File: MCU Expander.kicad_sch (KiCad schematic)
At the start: 0 parts

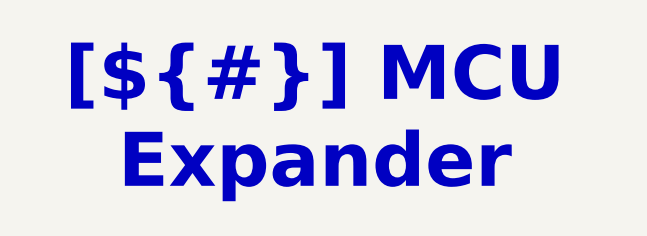
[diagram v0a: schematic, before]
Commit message: [Schematic][Add] Add of a new page : MCU Expander
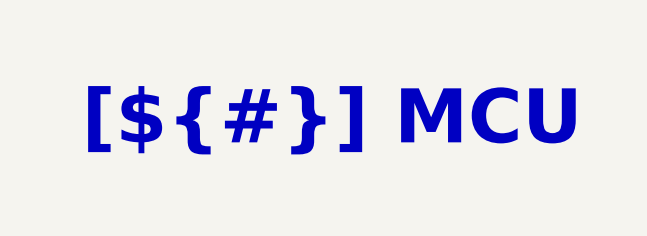
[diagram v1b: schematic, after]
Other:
- title: MCU Expander -> MCU
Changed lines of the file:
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@@
 	(paper "A4")
 	(title_block
-		(title "MCU Expander")
+		(title "MCU")
 		(date "2025-01-12")
 		(rev "${REVISION}")
@@
 	(text_box "[${#}] ${TITLE}"
 		(exclude_from_sim no)
-		(at 102.87 15.24 0)
-		(size 93.98 12.7)
+		(at 115.57 15.24 0)
+		(size 72.39 12.7)
 		(margins 4.4999 4.4999 4.4999 4.4999)
 		(stroke

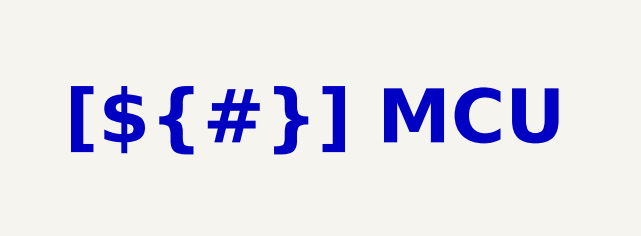
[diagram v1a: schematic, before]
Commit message: [Schematic][Add] MCU
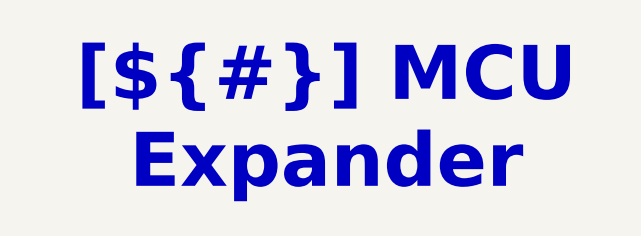
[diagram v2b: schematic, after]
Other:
- title: MCU -> MCU Expander
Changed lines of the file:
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@@
 	(paper "A4")
 	(title_block
-		(title "MCU")
+		(title "MCU Expander")
 		(date "2025-01-12")
 		(rev "${REVISION}")
@@
 	(text_box "[${#}] ${TITLE}"
 		(exclude_from_sim no)
-		(at 115.57 15.24 0)
-		(size 72.39 12.7)
+		(at 109.22 15.24 0)
+		(size 87.63 12.7)
 		(margins 4.4999 4.4999 4.4999 4.4999)
 		(stroke

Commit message: [Schematic][Add] MCU Expander Schematic
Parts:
- added C13, C15, C18: 100nF, Capacitor_SMD:C_0603_1608Metric_Pad1.08x0.95mm_HandSolder, symbol Device:C_Small
- added J2: *, Connector_Molex:Molex_Micro-Fit_3.0_43045-0612_2x03_P3.00mm_Vertical, symbol Connector_Generic:Conn_02x03_Odd_Even
- added R13: 10k, Resistor_SMD:R_0603_1608Metric_Pad0.98x0.95mm_HandSolder, symbol Device:R_Small
- added U2: TCAL9539, Package_SO:TSSOP-24_4.4x7.8mm_P0.65mm, symbol P_Interface:TCA9535PWR
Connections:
- new net +3.3V: C13.1, C18.1, J2.2 (Pin_2), R13.2, U2.24 (VCC)
- new net +5V: C15.1, J2.4 (Pin_4)
- new net CD_RELAY1: U2.10 (P06)
- new net CD_RELAY2: U2.11 (P07)
- new net GND: C13.2, C15.2, C18.2, J2.6 (Pin_6), U2.12 (GND), U2.2 (A1), U2.21 (A0)
- new net GPIO_EXP_P14: U2.17 (P14)
- new net GPIO_EXP_P15: U2.18 (P15)
- new net GPIO_EXP_P16: U2.19 (P16)
- new net GPIO_EXP_P17: U2.20 (P17)
- new net GPIO_Expander_~{INT}: U2.1 (~{INT})
- new net GPIO_Expander_~{RESET}: R13.1, U2.3 (~{RESET})
- new net I2C2_SCL: U2.22 (SCL)
- new net I2C2_SDA: U2.23 (SDA)
- new net IMU_SENSOR_INT1: U2.4 (P00)
- new net IMU_SENSOR_INT2: U2.5 (P01)
- new net Light_SENSOR_INT: U2.6 (P02)
- new net MCU_SPARE1: J2.1 (Pin_1)
- new net MCU_SPARE2: J2.3 (Pin_3)
- new net MicroSD_Detection: U2.7 (P03)
- new net RS485_DE: U2.9 (P05)
- new net RS485_~{RE}: U2.8 (P04)
- new net Switch_DIP_1: U2.13 (P10)
- new net Switch_DIP_2: U2.14 (P11)
- new net Switch_DIP_3: U2.15 (P12)
- new net Switch_DIP_4: U2.16 (P13)
- no-connect marks 0 -> 1

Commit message: [Schematic][Modify] Clear all annotation
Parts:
- renumbered C18 to C?, C13 to C?, C15 to C?, J2 to J?, R13 to R?, U2 to U?
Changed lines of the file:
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@@
 		(on_board yes)
 		(dnp no)
-		(property "Reference" "#PWR049"
+		(property "Reference" "#PWR?"
 			(at 195.58 130.81 0)
 			(effects
@@
 			(project "Data-Acquisition-Board"
 				(path "/f9e05184-c88b-4a88-ae9c-ab2bdb32be7c/c5103ceb-5325-4a84-a025-9638a412984e/6ab43cd8-dabb-49a4-aa94-5d820261f9f9"
-					(reference "#PWR049")
+					(reference "#PWR?")
 					(unit 1)
 				)
@@
 		(on_board yes)
 		(dnp no)
-		(property "Reference" "#PWR024"
+		(property "Reference" "#PWR?"
 			(at 99.06 76.2 0)
 			(effects
@@
 			(project "Data-Acquisition-Board"
 				(path "/f9e05184-c88b-4a88-ae9c-ab2bdb32be7c/c5103ceb-5325-4a84-a025-9638a412984e/6ab43cd8-dabb-49a4-aa94-5d820261f9f9"
-					(reference "#PWR024")
+					(reference "#PWR?")
 					(unit 1)
 				)
@@
 		(on_board yes)
 		(dnp no)
-		(property "Reference" "#PWR032"
+		(property "Reference" "#PWR?"
 			(at 110.49 74.93 0)
 			(effects
@@
 			(project "Data-Acquisition-Board"
 				(path "/f9e05184-c88b-4a88-ae9c-ab2bdb32be7c/c5103ceb-5325-4a84-a025-9638a412984e/6ab43cd8-dabb-49a4-aa94-5d820261f9f9"
-					(reference "#PWR032")
+					(reference "#PWR?")
 					(unit 1)
 				)
@@
 		(on_board yes)
 		(dnp no)
-		(property "Reference" "#PWR047"
+		(property "Reference" "#PWR?"
 			(at 176.53 63.5 0)
 			(effects
@@
 			(project "Data-Acquisition-Board"
 				(path "/f9e05184-c88b-4a88-ae9c-ab2bdb32be7c/c5103ceb-5325-4a84-a025-9638a412984e/6ab43cd8-dabb-49a4-aa94-5d820261f9f9"
-					(reference "#PWR047")
+					(reference "#PWR?")
 					(unit 1)
 				)
@@
 		(on_board yes)
 		(dnp no)
-		(property "Reference" "R13"
+		(property "Reference" "R?"
 			(at 172.466 86.36 0)
 			(effects
@@
 			(project "Data-Acquisition-Board"
 				(path "/f9e05184-c88b-4a88-ae9c-ab2bdb32be7c/c5103ceb-5325-4a84-a025-9638a412984e/6ab43cd8-dabb-49a4-aa94-5d820261f9f9"
-					(reference "R13")
+					(reference "R?")
 					(unit 1)
 				)
@@
 		(on_board yes)
 		(dnp no)
-		(property "Reference" "#PWR048"
+		(property "Reference" "#PWR?"
 			(at 195.58 64.77 0)
 			(effects
@@
 			(project "Data-Acquisition-Board"
 				(path "/f9e05184-c88b-4a88-ae9c-ab2bdb32be7c/c5103ceb-5325-4a84-a025-9638a412984e/6ab43cd8-dabb-49a4-aa94-5d820261f9f9"
-					(reference "#PWR048")
+					(reference "#PWR?")
 					(unit 1)
 				)
@@
 		(on_board yes)
 		(dnp no)
-		(property "Reference" "J2"
+		(property "Reference" "J?"
 			(at 91.44 58.42 0)
 			(effects
@@
 			(project "Data-Acquisition-Board"
 				(path "/f9e05184-c88b-4a88-ae9c-ab2bdb32be7c/c5103ceb-5325-4a84-a025-9638a412984e/6ab43cd8-dabb-49a4-aa94-5d820261f9f9"
-					(reference "J2")
+					(reference "J?")
 					(unit 1)
 				)
@@
 		(on_board yes)
 		(dnp no)
-		(property "Reference" "#PWR028"
+		(property "Reference" "#PWR?"
 			(at 104.14 66.04 0)
 			(effects
@@
 			(project "Data-Acquisition-Board"
 				(path "/f9e05184-c88b-4a88-ae9c-ab2bdb32be7c/c5103ceb-5325-4a84-a025-9638a412984e/6ab43cd8-dabb-49a4-aa94-5d820261f9f9"
-					(reference "#PWR028")
+					(reference "#PWR?")
 					(unit 1)
 				)
@@
 		(on_board yes)
 		(dnp no)
-		(property "Reference" "#PWR031"
+		(property "Reference" "#PWR?"
 			(at 110.49 63.5 0)
 			(effects
@@
 			(project "Data-Acquisition-Board"
 				(path "/f9e05184-c88b-4a88-ae9c-ab2bdb32be7c/c5103ceb-5325-4a84-a025-9638a412984e/6ab43cd8-dabb-49a4-aa94-5d820261f9f9"
-					(reference "#PWR031")
+					(reference "#PWR?")
 					(unit 1)
 				)
@@
 		(on_board yes)
 		(dnp no)
-		(property "Reference" "#PWR046"
+		(property "Reference" "#PWR?"
 			(at 175.26 130.81 0)
 			(effects
@@
 			(project "Data-Acquisition-Board"
 				(path "/f9e05184-c88b-4a88-ae9c-ab2bdb32be7c/c5103ceb-5325-4a84-a025-9638a412984e/6ab43cd8-dabb-49a4-aa94-5d820261f9f9"
-					(reference "#PWR046")
+					(reference "#PWR?")
 					(unit 1)
 				)
@@
 		(on_board yes)
 		(dnp no)
-		(property "Reference" "#PWR023"
+		(property "Reference" "#PWR?"
 			(at 99.06 66.04 0)
 			(effects
@@
 			(project "Data-Acquisition-Board"
 				(path "/f9e05184-c88b-4a88-ae9c-ab2bdb32be7c/c5103ceb-5325-4a84-a025-9638a412984e/6ab43cd8-dabb-49a4-aa94-5d820261f9f9"
-					(reference "#PWR023")
+					(reference "#PWR?")
 					(unit 1)
 				)
@@
 		(on_board yes)
 		(dnp no)
-		(property "Reference" "#PWR037"
+		(property "Reference" "#PWR?"
 			(at 123.19 74.93 0)
 			(effects
@@
 			(project "Data-Acquisition-Board"
 				(path "/f9e05184-c88b-4a88-ae9c-ab2bdb32be7c/c5103ceb-5325-4a84-a025-9638a412984e/6ab43cd8-dabb-49a4-aa94-5d820261f9f9"
-					(reference "#PWR037")
+					(reference "#PWR?")
 					(unit 1)
 				)
@@
 		(on_board yes)
 		(dnp no)
-		(property "Reference" "#PWR036"
+		(property "Reference" "#PWR?"
 			(at 123.19 63.5 0)
 			(effects
@@
 			(project "Data-Acquisition-Board"
 				(path "/f9e05184-c88b-4a88-ae9c-ab2bdb32be7c/c5103ceb-5325-4a84-a025-9638a412984e/6ab43cd8-dabb-49a4-aa94-5d820261f9f9"
-					(reference "#PWR036")
+					(reference "#PWR?")
 					(unit 1)
 				)
@@
 		(on_board yes)
 		(dnp no)
-		(property "Reference" "C18"
+		(property "Reference" "C?"
 			(at 186.69 60.452 90)
 			(effects
@@
 			(project "Data-Acquisition-Board"
 				(path "/f9e05184-c88b-4a88-ae9c-ab2bdb32be7c/c5103ceb-5325-4a84-a025-9638a412984e/6ab43cd8-dabb-49a4-aa94-5d820261f9f9"
-					(reference "C18")
+					(reference "C?")
 					(unit 1)
 				)
@@
 		(dnp no)
 		(fields_autoplaced yes)
-		(property "Reference" "U2"
+		(property "Reference" "U?"
 			(at 197.7233 66.04 0)
 			(effects
@@
 			(project "Data-Acquisition-Board"
 				(path "/f9e05184-c88b-4a88-ae9c-ab2bdb32be7c/c5103ceb-5325-4a84-a025-9638a412984e/6ab43cd8-dabb-49a4-aa94-5d820261f9f9"
-					(reference "U2")
+					(reference "U?")
 					(unit 1)
 				)
@@
 		(on_board yes)
 		(dnp no)
-		(property "Reference" "C13"
+		(property "Reference" "C?"
 			(at 112.268 63.5 0)
 			(effects
@@
 			(project "Data-Acquisition-Board"
 				(path "/f9e05184-c88b-4a88-ae9c-ab2bdb32be7c/c5103ceb-5325-4a84-a025-9638a412984e/6ab43cd8-dabb-49a4-aa94-5d820261f9f9"
-					(reference "C13")
+					(reference "C?")
 					(unit 1)
 				)
@@
 		(on_board yes)
 		(dnp no)
-		(property "Reference" "C15"
+		(property "Reference" "C?"
 			(at 124.968 63.5 0)
 			(effects
@@
 			(project "Data-Acquisition-Board"
 				(path "/f9e05184-c88b-4a88-ae9c-ab2bdb32be7c/c5103ceb-5325-4a84-a025-9638a412984e/6ab43cd8-dabb-49a4-aa94-5d820261f9f9"
-					(reference "C15")
+					(reference "C?")
 					(unit 1)
 				)
@@
 		(on_board yes)
 		(dnp no)
-		(property "Reference" "#PWR045"
+		(property "Reference" "#PWR?"
 			(at 175.26 86.36 0)
 			(effects
@@
 			(project "Data-Acquisition-Board"
 				(path "/f9e05184-c88b-4a88-ae9c-ab2bdb32be7c/c5103ceb-5325-4a84-a025-9638a412984e/6ab43cd8-dabb-49a4-aa94-5d820261f9f9"
-					(reference "#PWR045")
-					(unit 1)
-				)
+					(reference "#PWR?")
+					(unit 1)
+				)

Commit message: [Schematic][Modify] Annotation of all  the components
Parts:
- gave numbers to parts that had none: 6
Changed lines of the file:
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@@
 		(on_board yes)
 		(dnp no)
-		(property "Reference" "#PWR?"
+		(property "Reference" "#PWR049"
 			(at 195.58 130.81 0)
 			(effects
@@
 			(project "Data-Acquisition-Board"
 				(path "/f9e05184-c88b-4a88-ae9c-ab2bdb32be7c/c5103ceb-5325-4a84-a025-9638a412984e/6ab43cd8-dabb-49a4-aa94-5d820261f9f9"
-					(reference "#PWR?")
+					(reference "#PWR049")
 					(unit 1)
 				)
@@
 		(on_board yes)
 		(dnp no)
-		(property "Reference" "#PWR?"
+		(property "Reference" "#PWR039"
 			(at 99.06 76.2 0)
 			(effects
@@
 			(project "Data-Acquisition-Board"
 				(path "/f9e05184-c88b-4a88-ae9c-ab2bdb32be7c/c5103ceb-5325-4a84-a025-9638a412984e/6ab43cd8-dabb-49a4-aa94-5d820261f9f9"
-					(reference "#PWR?")
+					(reference "#PWR039")
 					(unit 1)
 				)
@@
 		(on_board yes)
 		(dnp no)
-		(property "Reference" "#PWR?"
+		(property "Reference" "#PWR042"
 			(at 110.49 74.93 0)
 			(effects
@@
 			(project "Data-Acquisition-Board"
 				(path "/f9e05184-c88b-4a88-ae9c-ab2bdb32be7c/c5103ceb-5325-4a84-a025-9638a412984e/6ab43cd8-dabb-49a4-aa94-5d820261f9f9"
-					(reference "#PWR?")
+					(reference "#PWR042")
 					(unit 1)
 				)
@@
 		(on_board yes)
 		(dnp no)
-		(property "Reference" "#PWR?"
+		(property "Reference" "#PWR047"
 			(at 176.53 63.5 0)
 			(effects
@@
 			(project "Data-Acquisition-Board"
 				(path "/f9e05184-c88b-4a88-ae9c-ab2bdb32be7c/c5103ceb-5325-4a84-a025-9638a412984e/6ab43cd8-dabb-49a4-aa94-5d820261f9f9"
-					(reference "#PWR?")
+					(reference "#PWR047")
 					(unit 1)
 				)
@@
 		(on_board yes)
 		(dnp no)
-		(property "Reference" "R?"
+		(property "Reference" "R13"
 			(at 172.466 86.36 0)
 			(effects
@@
 			(project "Data-Acquisition-Board"
 				(path "/f9e05184-c88b-4a88-ae9c-ab2bdb32be7c/c5103ceb-5325-4a84-a025-9638a412984e/6ab43cd8-dabb-49a4-aa94-5d820261f9f9"
-					(reference "R?")
+					(reference "R13")
 					(unit 1)
 				)
@@
 		(on_board yes)
 		(dnp no)
-		(property "Reference" "#PWR?"
+		(property "Reference" "#PWR048"
 			(at 195.58 64.77 0)
 			(effects
@@
 			(project "Data-Acquisition-Board"
 				(path "/f9e05184-c88b-4a88-ae9c-ab2bdb32be7c/c5103ceb-5325-4a84-a025-9638a412984e/6ab43cd8-dabb-49a4-aa94-5d820261f9f9"
-					(reference "#PWR?")
+					(reference "#PWR048")
 					(unit 1)
 				)
@@
 		(on_board yes)
 		(dnp no)
-		(property "Reference" "J?"
+		(property "Reference" "J4"
 			(at 91.44 58.42 0)
 			(effects
@@
 			(project "Data-Acquisition-Board"
 				(path "/f9e05184-c88b-4a88-ae9c-ab2bdb32be7c/c5103ceb-5325-4a84-a025-9638a412984e/6ab43cd8-dabb-49a4-aa94-5d820261f9f9"
-					(reference "J?")
+					(reference "J4")
 					(unit 1)
 				)
@@
 		(on_board yes)
 		(dnp no)
-		(property "Reference" "#PWR?"
+		(property "Reference" "#PWR040"
 			(at 104.14 66.04 0)
 			(effects
@@
 			(project "Data-Acquisition-Board"
 				(path "/f9e05184-c88b-4a88-ae9c-ab2bdb32be7c/c5103ceb-5325-4a84-a025-9638a412984e/6ab43cd8-dabb-49a4-aa94-5d820261f9f9"
-					(reference "#PWR?")
+					(reference "#PWR040")
 					(unit 1)
 				)
@@
 		(on_board yes)
 		(dnp no)
-		(property "Reference" "#PWR?"
+		(property "Reference" "#PWR041"
 			(at 110.49 63.5 0)
 			(effects
@@
 			(project "Data-Acquisition-Board"
 				(path "/f9e05184-c88b-4a88-ae9c-ab2bdb32be7c/c5103ceb-5325-4a84-a025-9638a412984e/6ab43cd8-dabb-49a4-aa94-5d820261f9f9"
-					(reference "#PWR?")
+					(reference "#PWR041")
 					(unit 1)
 				)
@@
 		(on_board yes)
 		(dnp no)
-		(property "Reference" "#PWR?"
+		(property "Reference" "#PWR046"
 			(at 175.26 130.81 0)
 			(effects
@@
 			(project "Data-Acquisition-Board"
 				(path "/f9e05184-c88b-4a88-ae9c-ab2bdb32be7c/c5103ceb-5325-4a84-a025-9638a412984e/6ab43cd8-dabb-49a4-aa94-5d820261f9f9"
-					(reference "#PWR?")
+					(reference "#PWR046")
 					(unit 1)
 				)
@@
 		(on_board yes)
 		(dnp no)
-		(property "Reference" "#PWR?"
+		(property "Reference" "#PWR038"
 			(at 99.06 66.04 0)
 			(effects
@@
 			(project "Data-Acquisition-Board"
 				(path "/f9e05184-c88b-4a88-ae9c-ab2bdb32be7c/c5103ceb-5325-4a84-a025-9638a412984e/6ab43cd8-dabb-49a4-aa94-5d820261f9f9"
-					(reference "#PWR?")
+					(reference "#PWR038")
 					(unit 1)
 				)
@@
 		(on_board yes)
 		(dnp no)
-		(property "Reference" "#PWR?"
+		(property "Reference" "#PWR044"
 			(at 123.19 74.93 0)
 			(effects
@@
 			(project "Data-Acquisition-Board"
 				(path "/f9e05184-c88b-4a88-ae9c-ab2bdb32be7c/c5103ceb-5325-4a84-a025-9638a412984e/6ab43cd8-dabb-49a4-aa94-5d820261f9f9"
-					(reference "#PWR?")
+					(reference "#PWR044")
 					(unit 1)
 				)
@@
 		(on_board yes)
 		(dnp no)
-		(property "Reference" "#PWR?"
+		(property "Reference" "#PWR043"
 			(at 123.19 63.5 0)
 			(effects
@@
 			(project "Data-Acquisition-Board"
 				(path "/f9e05184-c88b-4a88-ae9c-ab2bdb32be7c/c5103ceb-5325-4a84-a025-9638a412984e/6ab43cd8-dabb-49a4-aa94-5d820261f9f9"
-					(reference "#PWR?")
+					(reference "#PWR043")
 					(unit 1)
 				)
@@
 		(on_board yes)
 		(dnp no)
-		(property "Reference" "C?"
+		(property "Reference" "C18"
 			(at 186.69 60.452 90)
 			(effects
@@
 			(project "Data-Acquisition-Board"
 				(path "/f9e05184-c88b-4a88-ae9c-ab2bdb32be7c/c5103ceb-5325-4a84-a025-9638a412984e/6ab43cd8-dabb-49a4-aa94-5d820261f9f9"
-					(reference "C?")
+					(reference "C18")
 					(unit 1)
 				)
@@
 		(dnp no)
 		(fields_autoplaced yes)
-		(property "Reference" "U?"
+		(property "Reference" "U2"
 			(at 197.7233 66.04 0)
 			(effects
@@
 			(project "Data-Acquisition-Board"
 				(path "/f9e05184-c88b-4a88-ae9c-ab2bdb32be7c/c5103ceb-5325-4a84-a025-9638a412984e/6ab43cd8-dabb-49a4-aa94-5d820261f9f9"
-					(reference "U?")
+					(reference "U2")
 					(unit 1)
 				)
@@
 		(on_board yes)
 		(dnp no)
-		(property "Reference" "C?"
+		(property "Reference" "C16"
 			(at 112.268 63.5 0)
 			(effects
@@
 			(project "Data-Acquisition-Board"
 				(path "/f9e05184-c88b-4a88-ae9c-ab2bdb32be7c/c5103ceb-5325-4a84-a025-9638a412984e/6ab43cd8-dabb-49a4-aa94-5d820261f9f9"
-					(reference "C?")
+					(reference "C16")
 					(unit 1)
 				)
@@
 		(on_board yes)
 		(dnp no)
-		(property "Reference" "C?"
+		(property "Reference" "C17"
 			(at 124.968 63.5 0)
 			(effects
@@
 			(project "Data-Acquisition-Board"
 				(path "/f9e05184-c88b-4a88-ae9c-ab2bdb32be7c/c5103ceb-5325-4a84-a025-9638a412984e/6ab43cd8-dabb-49a4-aa94-5d820261f9f9"
-					(reference "C?")
+					(reference "C17")
 					(unit 1)
 				)
@@
 		(on_board yes)
 		(dnp no)
-		(property "Reference" "#PWR?"
+		(property "Reference" "#PWR045"
 			(at 175.26 86.36 0)
 			(effects
@@
 			(project "Data-Acquisition-Board"
 				(path "/f9e05184-c88b-4a88-ae9c-ab2bdb32be7c/c5103ceb-5325-4a84-a025-9638a412984e/6ab43cd8-dabb-49a4-aa94-5d820261f9f9"
-					(reference "#PWR?")
-					(unit 1)
-				)
+					(reference "#PWR045")
+					(unit 1)
+				)

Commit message: [Schematic][Modify] Annotation of all  the components
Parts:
- renumbered C18 to C16, C16 to C17, C17 to C18
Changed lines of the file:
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@@
 		(on_board yes)
 		(dnp no)
-		(property "Reference" "#PWR039"
+		(property "Reference" "#PWR046"
 			(at 99.06 76.2 0)
 			(effects
@@
 			(project "Data-Acquisition-Board"
 				(path "/f9e05184-c88b-4a88-ae9c-ab2bdb32be7c/c5103ceb-5325-4a84-a025-9638a412984e/6ab43cd8-dabb-49a4-aa94-5d820261f9f9"
-					(reference "#PWR039")
+					(reference "#PWR046")
 					(unit 1)
 				)
@@
 		(on_board yes)
 		(dnp no)
-		(property "Reference" "#PWR042"
+		(property "Reference" "#PWR044"
 			(at 110.49 74.93 0)
 			(effects
@@
 			(project "Data-Acquisition-Board"
 				(path "/f9e05184-c88b-4a88-ae9c-ab2bdb32be7c/c5103ceb-5325-4a84-a025-9638a412984e/6ab43cd8-dabb-49a4-aa94-5d820261f9f9"
-					(reference "#PWR042")
+					(reference "#PWR044")
 					(unit 1)
 				)
@@
 		(on_board yes)
 		(dnp no)
-		(property "Reference" "#PWR047"
+		(property "Reference" "#PWR043"
 			(at 176.53 63.5 0)
 			(effects
@@
 			(project "Data-Acquisition-Board"
 				(path "/f9e05184-c88b-4a88-ae9c-ab2bdb32be7c/c5103ceb-5325-4a84-a025-9638a412984e/6ab43cd8-dabb-49a4-aa94-5d820261f9f9"
-					(reference "#PWR047")
+					(reference "#PWR043")
 					(unit 1)
 				)
@@
 		(on_board yes)
 		(dnp no)
-		(property "Reference" "#PWR048"
+		(property "Reference" "#PWR040"
 			(at 195.58 64.77 0)
 			(effects
@@
 			(project "Data-Acquisition-Board"
 				(path "/f9e05184-c88b-4a88-ae9c-ab2bdb32be7c/c5103ceb-5325-4a84-a025-9638a412984e/6ab43cd8-dabb-49a4-aa94-5d820261f9f9"
-					(reference "#PWR048")
+					(reference "#PWR040")
 					(unit 1)
 				)
@@
 		(on_board yes)
 		(dnp no)
-		(property "Reference" "#PWR040"
+		(property "Reference" "#PWR042"
 			(at 104.14 66.04 0)
 			(effects
@@
 			(project "Data-Acquisition-Board"
 				(path "/f9e05184-c88b-4a88-ae9c-ab2bdb32be7c/c5103ceb-5325-4a84-a025-9638a412984e/6ab43cd8-dabb-49a4-aa94-5d820261f9f9"
-					(reference "#PWR040")
+					(reference "#PWR042")
 					(unit 1)
 				)
@@
 		(on_board yes)
 		(dnp no)
-		(property "Reference" "#PWR041"
+		(property "Reference" "#PWR038"
 			(at 110.49 63.5 0)
 			(effects
@@
 			(project "Data-Acquisition-Board"
 				(path "/f9e05184-c88b-4a88-ae9c-ab2bdb32be7c/c5103ceb-5325-4a84-a025-9638a412984e/6ab43cd8-dabb-49a4-aa94-5d820261f9f9"
-					(reference "#PWR041")
+					(reference "#PWR038")
 					(unit 1)
 				)
@@
 		(on_board yes)
 		(dnp no)
-		(property "Reference" "#PWR046"
+		(property "Reference" "#PWR048"
 			(at 175.26 130.81 0)
 			(effects
@@
 			(project "Data-Acquisition-Board"
 				(path "/f9e05184-c88b-4a88-ae9c-ab2bdb32be7c/c5103ceb-5325-4a84-a025-9638a412984e/6ab43cd8-dabb-49a4-aa94-5d820261f9f9"
-					(reference "#PWR046")
+					(reference "#PWR048")
 					(unit 1)
 				)
@@
 		(on_board yes)
 		(dnp no)
-		(property "Reference" "#PWR038"
+		(property "Reference" "#PWR041"
 			(at 99.06 66.04 0)
 			(effects
@@
 			(project "Data-Acquisition-Board"
 				(path "/f9e05184-c88b-4a88-ae9c-ab2bdb32be7c/c5103ceb-5325-4a84-a025-9638a412984e/6ab43cd8-dabb-49a4-aa94-5d820261f9f9"
-					(reference "#PWR038")
+					(reference "#PWR041")
 					(unit 1)
 				)
@@
 		(on_board yes)
 		(dnp no)
-		(property "Reference" "#PWR044"
+		(property "Reference" "#PWR045"
 			(at 123.19 74.93 0)
 			(effects
@@
 			(project "Data-Acquisition-Board"
 				(path "/f9e05184-c88b-4a88-ae9c-ab2bdb32be7c/c5103ceb-5325-4a84-a025-9638a412984e/6ab43cd8-dabb-49a4-aa94-5d820261f9f9"
-					(reference "#PWR044")
+					(reference "#PWR045")
 					(unit 1)
 				)
@@
 		(on_board yes)
 		(dnp no)
-		(property "Reference" "#PWR043"
+		(property "Reference" "#PWR039"
 			(at 123.19 63.5 0)
 			(effects
@@
 			(project "Data-Acquisition-Board"
 				(path "/f9e05184-c88b-4a88-ae9c-ab2bdb32be7c/c5103ceb-5325-4a84-a025-9638a412984e/6ab43cd8-dabb-49a4-aa94-5d820261f9f9"
-					(reference "#PWR043")
+					(reference "#PWR039")
 					(unit 1)
 				)
@@
 		(on_board yes)
 		(dnp no)
-		(property "Reference" "C18"
+		(property "Reference" "C16"
 			(at 186.69 60.452 90)
 			(effects
@@
 			(project "Data-Acquisition-Board"
 				(path "/f9e05184-c88b-4a88-ae9c-ab2bdb32be7c/c5103ceb-5325-4a84-a025-9638a412984e/6ab43cd8-dabb-49a4-aa94-5d820261f9f9"
-					(reference "C18")
+					(reference "C16")
 					(unit 1)
 				)
@@
 		(on_board yes)
 		(dnp no)
-		(property "Reference" "C16"
+		(property "Reference" "C17"
 			(at 112.268 63.5 0)
 			(effects
@@
 			(project "Data-Acquisition-Board"
 				(path "/f9e05184-c88b-4a88-ae9c-ab2bdb32be7c/c5103ceb-5325-4a84-a025-9638a412984e/6ab43cd8-dabb-49a4-aa94-5d820261f9f9"
-					(reference "C16")
+					(reference "C17")
 					(unit 1)
 				)
@@
 		(on_board yes)
 		(dnp no)
-		(property "Reference" "C17"
+		(property "Reference" "C18"
 			(at 124.968 63.5 0)
 			(effects
@@
 			(project "Data-Acquisition-Board"
 				(path "/f9e05184-c88b-4a88-ae9c-ab2bdb32be7c/c5103ceb-5325-4a84-a025-9638a412984e/6ab43cd8-dabb-49a4-aa94-5d820261f9f9"
-					(reference "C17")
+					(reference "C18")
 					(unit 1)
 				)
@@
 		(on_board yes)
 		(dnp no)
-		(property "Reference" "#PWR045"
+		(property "Reference" "#PWR047"
 			(at 175.26 86.36 0)
 			(effects
@@
 			(project "Data-Acquisition-Board"
 				(path "/f9e05184-c88b-4a88-ae9c-ab2bdb32be7c/c5103ceb-5325-4a84-a025-9638a412984e/6ab43cd8-dabb-49a4-aa94-5d820261f9f9"
-					(reference "#PWR045")
-					(unit 1)
-				)
+					(reference "#PWR047")
+					(unit 1)
+				)
